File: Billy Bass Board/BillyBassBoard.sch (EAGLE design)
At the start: 106 parts, among them J1 MICRO-USB-AB, J10 MPT-2-SCREW, J11 MPT-2-SCREW, J2 MPT-2-SCREW, J3 MICRO-SD, J4 MPT-2-SCREW, J5 JST-XH-2, J6 3.5MM-JACK-4-TIP, J7 JST-XH-2, J8 MPT-2-SCREW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

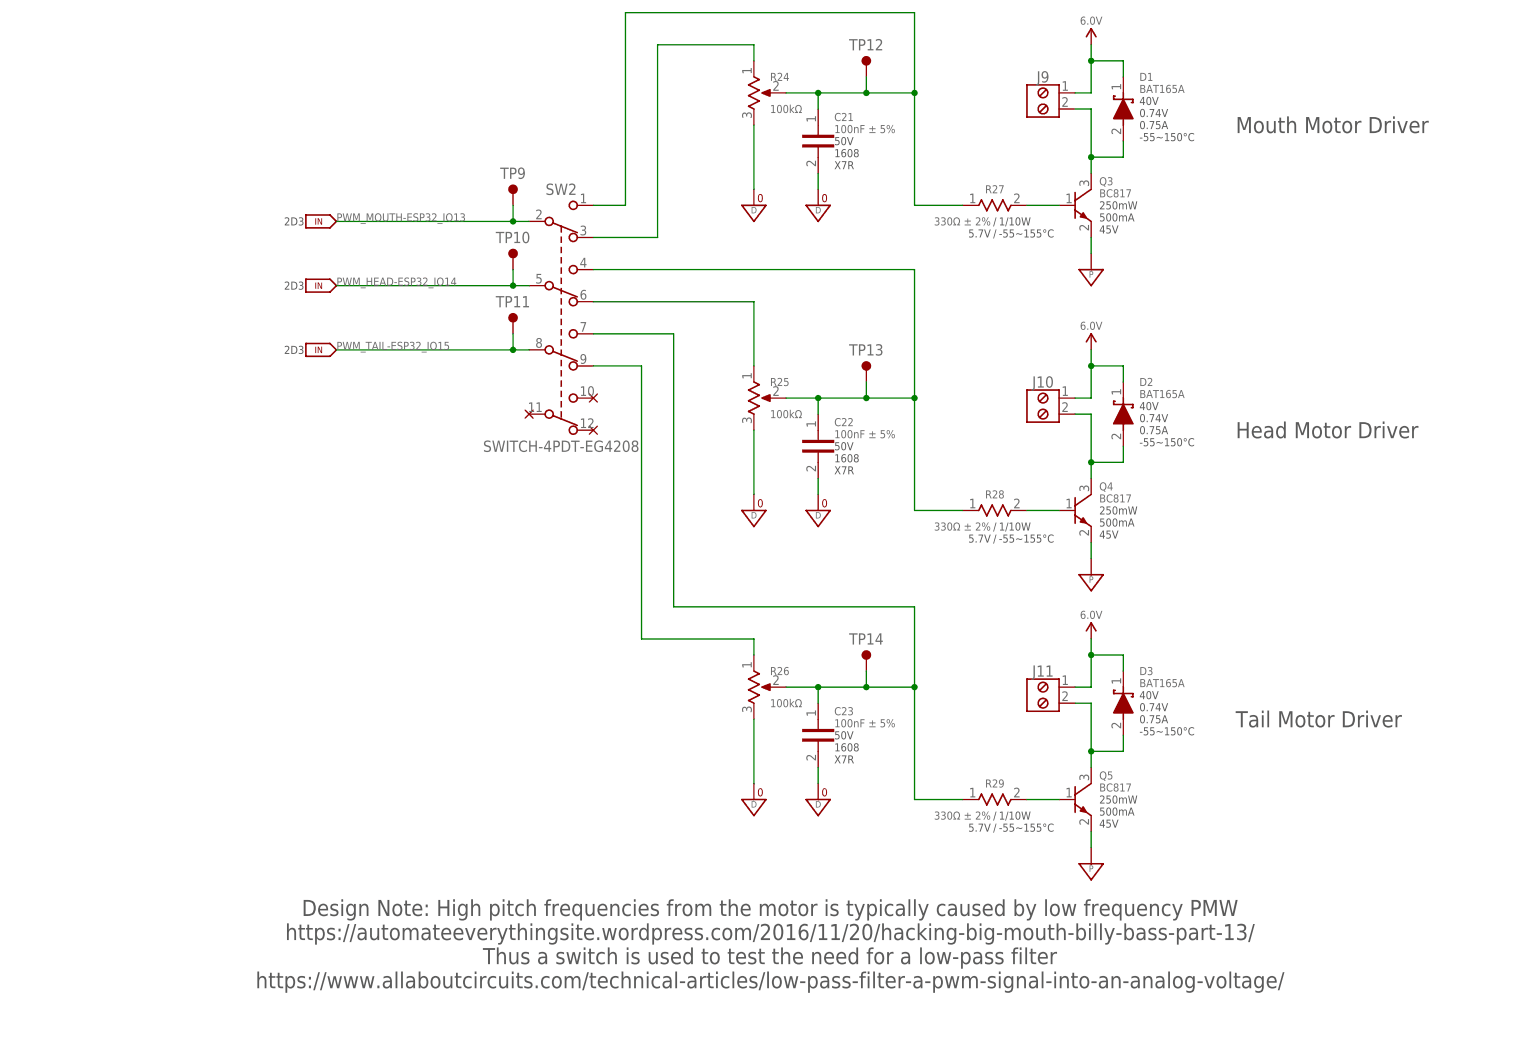
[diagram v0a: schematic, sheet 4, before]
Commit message: Updated files to match parts purchased
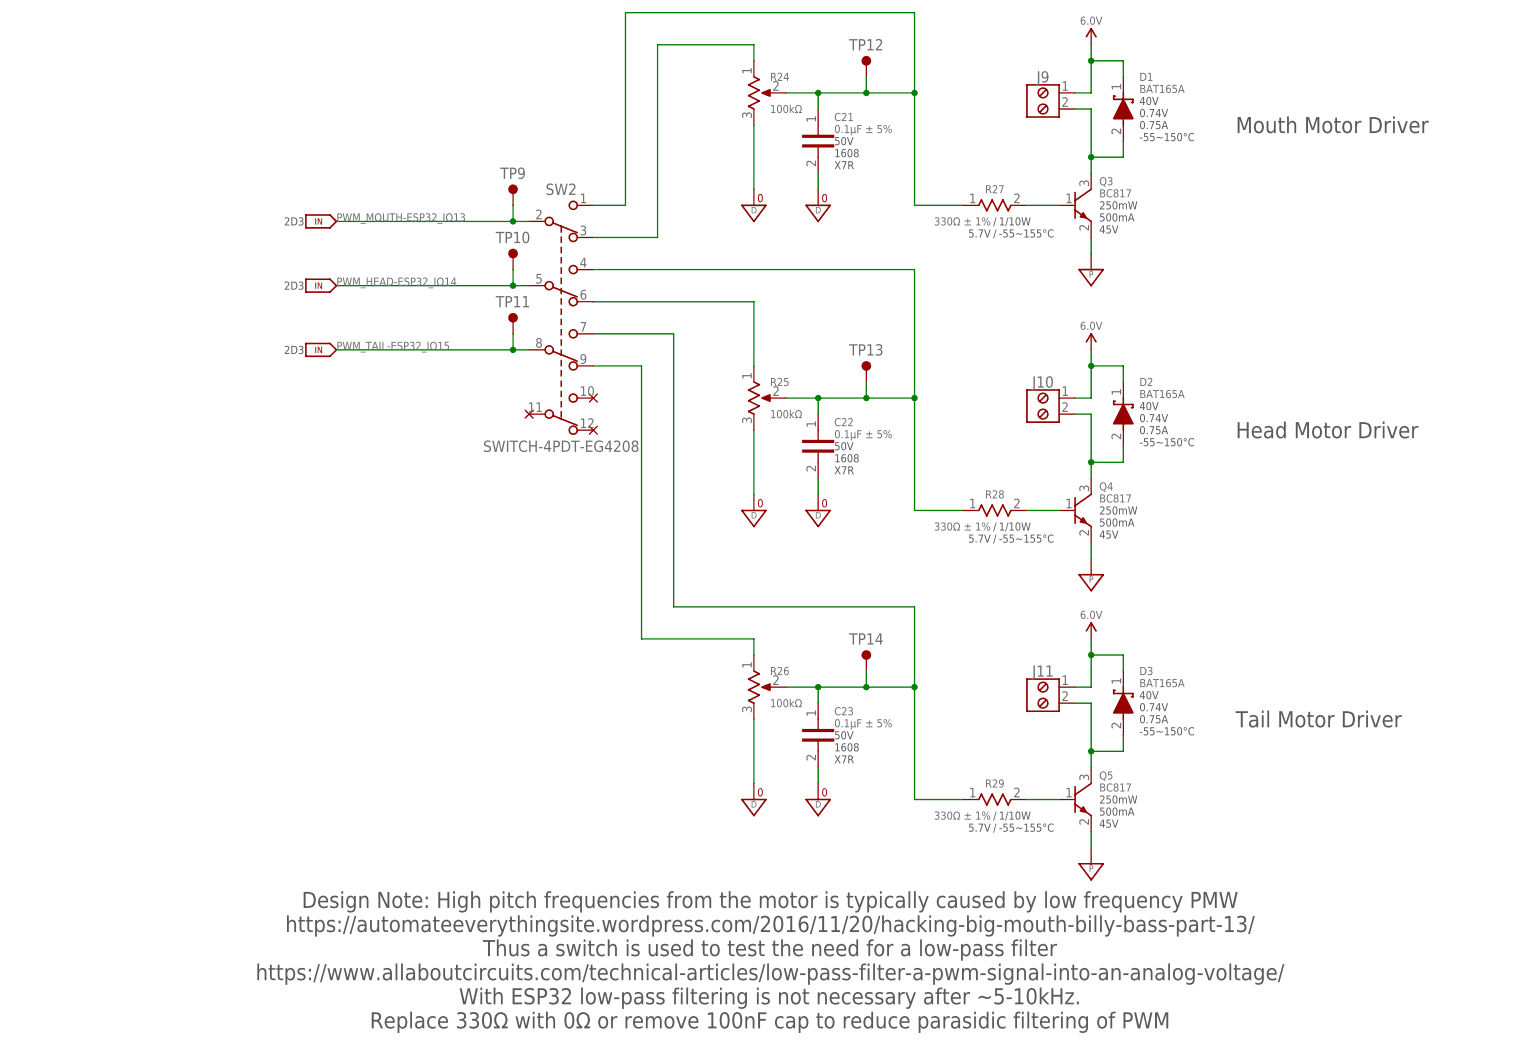
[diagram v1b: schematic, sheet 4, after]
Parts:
- C12, C20, C21, C22, C23, C28, C3, C5, C7, C9: value 100nF ± 5% -> 0.1µF ± 5%; device Harrington-Capacitors:CAP-V-100NF-1608 -> Harrington-Capacitors:CAP-V-0.1UF-1608
- C16: value 47nF ± 5% -> 0.047µF ± 10%; device Harrington-Capacitors:CAP-V-47NF-1608 -> Harrington-Capacitors:CAP-V-0.047UF-1608
- R13: value 1kΩ ± 2% -> 1kΩ ± 1%
- R17: value 10Ω ± 2% -> 10Ω ± 1%
- R22, R23: value 2.4kΩ ± 2% -> 2.4kΩ ± 1%
- R27, R28, R29: value 330Ω ± 2% -> 330Ω ± 1%
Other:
- note added: "Design Note: High pitch frequencies from the motor is typically caused by low frequency PMW https://automateeverythingsite.wordpress.com/2016/11/20/hacking-big-mouth-billy-bass-part-13/ Thus a switch is used to test the need for a low-pass filter https://www.allaboutcircuits.com/technical-articles/low-pass-filter-a-pwm-signal-into-an-analog-voltage/ With ESP32 low-pass filtering is not necessary 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"
- note removed: "Design Note: High pitch frequencies from the motor is typically caused by low frequency PMW https://automateeverythingsite.wordpress.com/2016/11/20/hacking-big-mouth-billy-bass-part-13/ Thus a switch is used to test the need for a low-pass filter https://www.allaboutcircuits.com/technical-articles/low-pass-filter-a-pwm-signal-into-an-analog-voltage/"
